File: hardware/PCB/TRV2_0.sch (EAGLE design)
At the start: 51 parts, among them IC1 TMP112, IC2 IC2, IC4 CNY70, IC5 ATMEGA8-AU, Q1 FC-12M, U1 DRV8850_RGY_24

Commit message: near done :-D
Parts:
- renumbered Q1 to X1
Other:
- note added: "ON BOM (14/10-2016)"
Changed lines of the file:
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@@
 <part name="GND23" library="supply1" deviceset="GND" device=""/>
 <part name="IC5" library="Arduino-AVR" deviceset="ATMEGA8" device="-AU"/>
-<part name="Q1" library="crystal" deviceset="FC-12M" device=""/>
+<part name="X1" library="crystal" deviceset="FC-12M" device=""/>
 <part name="C16" library="rcl" deviceset="C-EU" device="C0603" value="0p"/>
 <part name="C17" library="rcl" deviceset="C-EU" device="C0603" value="0p"/>
@@
 <text x="26.67" y="252.476" size="1.778" layer="95">IC2</text>
 <text x="26.162" y="225.044" size="1.778" layer="95">IC1</text>
+<text x="35.56" y="7.62" size="1.778" layer="94" rot="R180">ON BOM (14/10-2016)</text>
+<text x="71.12" y="251.46" size="1.778" layer="94" rot="R270">ON BOM (14/10-2016)</text>
+<text x="20.32" y="256.54" size="1.778" layer="94">ON BOM (14/10-2016)</text>
+<text x="71.12" y="223.52" size="1.778" layer="94" rot="R270">ON BOM (14/10-2016)</text>
+<text x="17.78" y="226.06" size="1.778" layer="94">ON BOM (14/10-2016)</text>
+<text x="106.68" y="228.6" size="1.778" layer="94">ON BOM (14/10-2016)</text>
+<text x="101.6" y="231.14" size="1.778" layer="94" rot="R270">ON BOM (14/10-2016)</text>
+<text x="134.62" y="256.54" size="1.778" layer="94" rot="R270">ON BOM (14/10-2016)</text>
+<text x="152.4" y="243.84" size="1.778" layer="94" rot="R270">ON BOM (14/10-2016)</text>
+<text x="177.8" y="243.84" size="1.778" layer="94" rot="R270">ON BOM (14/10-2016)</text>
+<text x="210.82" y="256.54" size="1.778" layer="94" rot="R270">ON BOM (14/10-2016)</text>
+<text x="233.68" y="228.6" size="1.778" layer="94" rot="R270">ON BOM (14/10-2016)</text>
+<text x="251.46" y="231.14" size="1.778" layer="94" rot="R270">ON BOM (14/10-2016)</text>
+<text x="279.4" y="246.38" size="1.778" layer="94" rot="R270">ON BOM (14/10-2016)</text>
+<text x="289.56" y="228.6" size="1.778" layer="94" rot="R270">ON BOM (14/10-2016)</text>
+<text x="327.66" y="248.92" size="1.778" layer="94">ON BOM (14/10-2016)</text>
+<text x="332.74" y="218.44" size="1.778" layer="94">ON BOM (14/10-2016)</text>
+<text x="330.2" y="210.82" size="1.778" layer="94">ON BOM (14/10-2016)</text>
+<text x="368.3" y="228.6" size="1.778" layer="94" rot="R90">ON BOM (14/10-2016)</text>
+<text x="22.86" y="182.88" size="1.778" layer="94" rot="R270">ON BOM (14/10-2016)</text>
+<text x="22.86" y="154.94" size="1.778" layer="94" rot="R270">ON BOM (14/10-2016)</text>
+<text x="35.56" y="149.86" size="1.778" layer="94">ON BOM (14/10-2016)</text>
+<text x="104.14" y="185.42" size="1.778" layer="94" rot="R270">ON BOM (14/10-2016)</text>
+<text x="238.76" y="167.64" size="1.778" layer="94" rot="R270">ON BOM (14/10-2016)</text>
+<text x="254" y="165.1" size="1.778" layer="94">ON BOM (14/10-2016)</text>
+<text x="254" y="152.4" size="1.778" layer="94">ON BOM (14/10-2016)</text>
+<text x="271.78" y="170.18" size="1.778" layer="94">ON BOM (14/10-2016)</text>
+<text x="327.66" y="162.56" size="1.778" layer="94" rot="R90">ON BOM (14/10-2016)</text>
+<text x="274.32" y="162.56" size="1.778" layer="94">ON BOM (14/10-2016)</text>
+<text x="88.9" y="109.22" size="1.778" layer="94" rot="R90">ON BOM (14/10-2016)</text>
+<text x="10.16" y="68.58" size="1.778" layer="94" rot="R270">ON BOM (14/10-2016)</text>
+<text x="40.64" y="68.58" size="1.778" layer="94" rot="R270">ON BOM (14/10-2016)</text>
+<text x="177.8" y="96.52" size="1.778" layer="94" rot="R270">ON BOM (14/10-2016)</text>
+<text x="177.8" y="66.04" size="1.778" layer="94" rot="R270">ON BOM (14/10-2016)</text>
+<text x="182.88" y="66.04" size="1.778" layer="94">ON BOM (14/10-2016)</text>
+<text x="43.18" y="55.88" size="1.778" layer="94">ON BOM (14/10-2016)</text>
+<text x="63.5" y="55.88" size="1.778" layer="94">ON BOM (14/10-2016)</text>
+<text x="55.88" y="66.04" size="1.778" layer="94">ON BOM (14/10-2016)</text>
+<text x="203.2" y="17.78" size="1.778" layer="94">ON BOM (14/10-2016)</text>
+<text x="58.42" y="25.4" size="1.778" layer="94" rot="R180">ON BOM (14/10-2016)</text>
+<text x="312.42" y="50.8" size="1.778" layer="94" rot="R180">ON BOM (14/10-2016)</text>
+<text x="83.82" y="182.88" size="1.778" layer="94" rot="R270">ON BOM (14/10-2016)</text>
+<text x="83.82" y="147.32" size="1.778" layer="94">ON BOM (14/10-2016)</text>
+<text x="33.02" y="172.72" size="1.778" layer="94">ON BOM (14/10-2016)</text>
+<text x="30.48" y="165.1" size="1.778" layer="94">ON BOM (14/10-2016)</text>
+<text x="33.02" y="157.48" size="1.778" layer="94">ON BOM (14/10-2016)</text>
+<text x="243.84" y="2.54" size="1.778" layer="94" rot="R90">ON BOM (14/10-2016)</text>
 </plain>
 <instances>
@@
 <instance part="GND23" gate="1" x="33.02" y="50.8"/>
 <instance part="IC5" gate="1" x="121.92" y="73.66"/>
-<instance part="Q1" gate="G$1" x="66.04" y="63.5"/>
+<instance part="X1" gate="G$1" x="66.04" y="63.5"/>
 <instance part="C16" gate="G$1" x="58.42" y="58.42"/>
 <instance part="C17" gate="G$1" x="73.66" y="58.42"/>
@@
 <net name="N$4" class="0">
 <segment>
-<pinref part="Q1" gate="G$1" pin="1"/>
+<pinref part="X1" gate="G$1" pin="1"/>
 <wire x1="63.5" y1="63.5" x2="58.42" y2="63.5" width="0.1524" layer="91"/>
 <pinref part="C16" gate="G$1" pin="1"/>
@@
 <net name="N$5" class="0">
 <segment>
-<pinref part="Q1" gate="G$1" pin="2"/>
+<pinref part="X1" gate="G$1" pin="2"/>
 <wire x1="68.58" y1="63.5" x2="73.66" y2="63.5" width="0.1524" layer="91"/>
 <pinref part="C17" gate="G$1" pin="1"/>

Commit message: ready for gerbers
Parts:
- added ML, MR: TPB1,27, testpad:TPB1,27
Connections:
- net ML: now also ML.TP
- net MR: now also MR.TP
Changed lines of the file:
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@@
 <part name="U$2" library="led" deviceset="KINGBRIGHTSIDELED" device=""/>
 <part name="GND19" library="SparkFun-Aesthetics" deviceset="GND" device=""/>
+<part name="ML" library="testpad" deviceset="TP" device="B1,27" value="TPB1,27"/>
+<part name="MR" library="testpad" deviceset="TP" device="B1,27" value="TPB1,27"/>
 </parts>
 <sheets>
@@
 <instance part="U$2" gate="G$1" x="236.22" y="7.62" smashed="yes" rot="R270"/>
 <instance part="GND19" gate="1" x="251.46" y="157.48"/>
+<instance part="ML" gate="G$1" x="167.64" y="99.06"/>
+<instance part="MR" gate="G$1" x="172.72" y="96.52"/>
 </instances>
 <busses>
@@
 <segment>
 <pinref part="IC5" gate="1" pin="ANALOG_2"/>
-<wire x1="152.4" y1="96.52" x2="160.02" y2="96.52" width="0.1524" layer="91"/>
+<wire x1="152.4" y1="96.52" x2="167.64" y2="96.52" width="0.1524" layer="91"/>
 <label x="157.48" y="96.52" size="1.778" layer="95"/>
+<pinref part="ML" gate="G$1" pin="TP"/>
+<wire x1="167.64" y1="96.52" x2="170.18" y2="96.52" width="0.1524" layer="91"/>
+<junction x="167.64" y="96.52"/>
 </segment>
 </net>
@@
 <segment>
 <pinref part="IC5" gate="1" pin="ANALOG_3"/>
-<wire x1="152.4" y1="93.98" x2="160.02" y2="93.98" width="0.1524" layer="91"/>
+<wire x1="152.4" y1="93.98" x2="172.72" y2="93.98" width="0.1524" layer="91"/>
 <label x="157.48" y="93.98" size="1.778" layer="95"/>
-</segment>
-</net>
+<pinref part="MR" gate="G$1" pin="TP"/>
+<wire x1="172.72" y1="93.98" x2="175.26" y2="93.98" width="0.1524" layer="91"/>
+<junction x="172.72" y="93.98"/>
+</segment>
+</net>

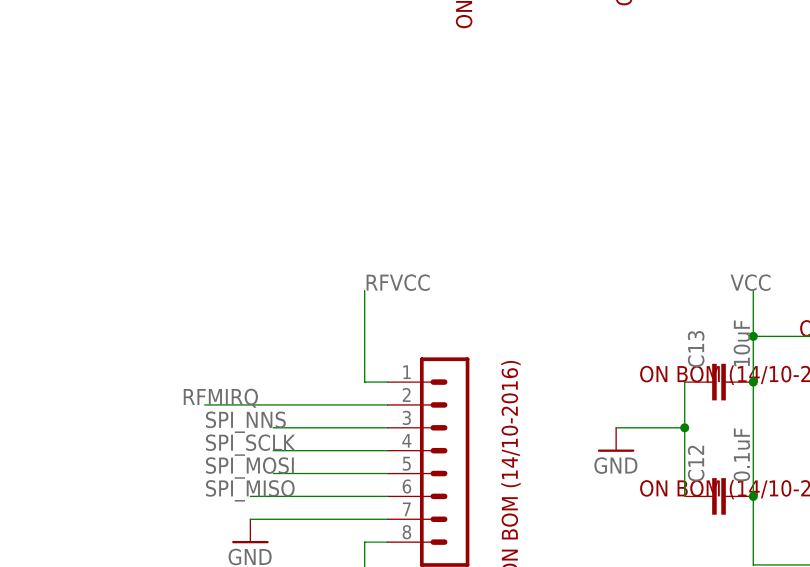
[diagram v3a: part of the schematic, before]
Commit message: added power to radio module connector
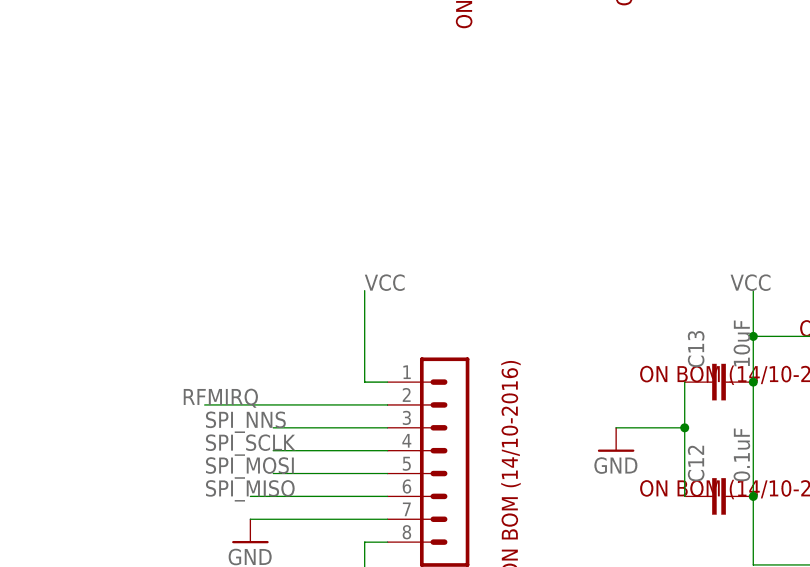
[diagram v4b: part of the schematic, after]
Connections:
- removed net RFVCC: J4.1
- net VCC: now also J4.1
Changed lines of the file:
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@@
 <junction x="266.7" y="170.18"/>
+</segment>
+<segment>
+<wire x1="226.06" y1="165.1" x2="223.52" y2="165.1" width="0.1524" layer="91"/>
+<wire x1="223.52" y1="165.1" x2="223.52" y2="175.26" width="0.1524" layer="91"/>
+<label x="223.52" y="175.26" size="1.778" layer="95"/>
+<pinref part="J4" gate="1" pin="1"/>
 </segment>
 </net>
@@
 </segment>
 </net>
-<net name="RFVCC" class="0">
-<segment>
-<wire x1="226.06" y1="165.1" x2="223.52" y2="165.1" width="0.1524" layer="91"/>
-<wire x1="223.52" y1="165.1" x2="223.52" y2="175.26" width="0.1524" layer="91"/>
-<label x="223.52" y="175.26" size="1.778" layer="95"/>
-<pinref part="J4" gate="1" pin="1"/>
-</segment>
-</net>
